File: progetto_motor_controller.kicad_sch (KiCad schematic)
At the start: 38 parts, among them J1 USB_B_Micro, J2 Conn_01x06, J3 Conn_01x04, J4 Screw_Terminal_01x03, J5 Conn_01x05, J6 Conn_02x10_Counter_Clockwise, J7 Conn_01x02, Q1 BSC022N04LSATMA1, SW1 SW_SPDT, U1 STM32F303RETx, U2 SN65HVD253D, U3 USBLC6-2P6, Y1 16MHz

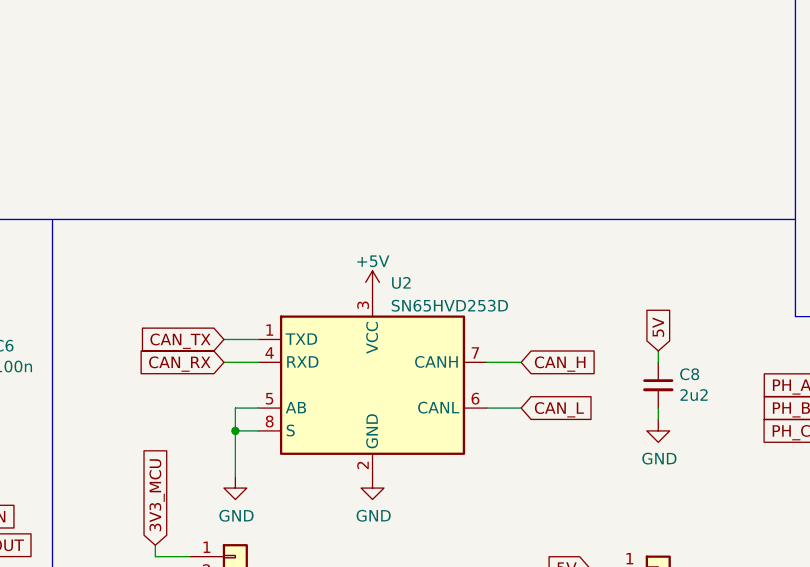
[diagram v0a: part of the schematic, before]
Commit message: added local symbol library
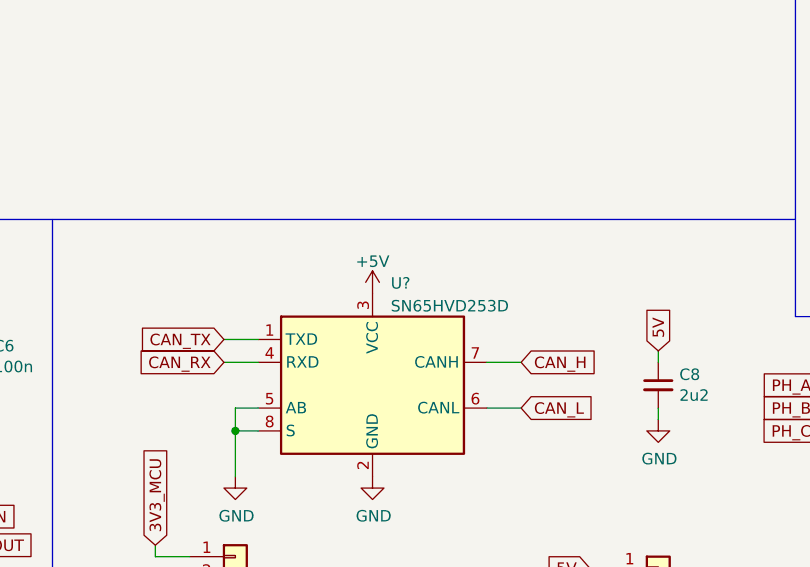
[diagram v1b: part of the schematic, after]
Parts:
- removed U2: SN65HVD253D, Package_SO:SOIC-8_3.9x4.9mm_P1.27mm, symbol Mylibrary:SN65HVD253D
- added U?: SN65HVD253D, Package_SO:SOIC-8_3.9x4.9mm_P1.27mm, symbol MyLibrary_PMSM:SN65HVD253D
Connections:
- net +5V: now also U?.3 (VCC)
- net CAN_H: now also U?.7 (CANH)
- net CAN_L: now also U?.6 (CANL)
- net CAN_RX: now also U?.4 (RXD)
- net CAN_TX: now also U?.1 (TXD)
- net GND: now also U?.2 (GND), U?.5 (NC), U?.8 (S)
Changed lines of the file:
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@@
     (pin "2")
   )
-  (symbol (lib_id "Mylibrary:SN65HVD253D") (at 149.86 90.17 0) (unit 1)
+  (symbol (lib_id "MyLibrary_PMSM:SN65HVD253D") (at 149.86 90.17 0) (unit 1)
     (in_bom yes) (on_board yes) (fields_autoplaced)
-    (property "Reference" "U2" (id 0) (at 151.8794 78.8502 0)
+    (property "Reference" "U?" (id 0) (at 151.8794 78.8502 0)
       (effects (font (size 1.27 1.27)) (justify left))
     )
@@
       (reference "U1") (unit 1) (value "STM32F303RETx") (footprint "Package_QFP:LQFP-64_10x10mm_P0.5mm")
     )
-    (path "/8331f48a-2afc-42bc-8008-84b452f97299"
-      (reference "U2") (unit 1) (value "SN65HVD253D") (footprint "Package_SO:SOIC-8_3.9x4.9mm_P1.27mm")
-    )
     (path "/00000000-0000-0000-0000-000061e1e007"
       (reference "U3") (unit 1) (value "USBLC6-2P6") (footprint "Package_TO_SOT_SMD:SOT-666")
     )
-    (path "/00000000-0000-0000-0000-000061cd02c2/00000000-0000-0000-0000-000061f8f6c5"
-      (reference "U4") (unit 1) (value "TMC6140") (footprint "")
-    )
-    (path "/00000000-0000-0000-0000-000061cd02c2/a6ec7d6b-e580-4409-8382-f30dedf5c393"
-      (reference "U5") (unit 1) (value "TSC2011") (footprint "")
-    )
-    (path "/00000000-0000-0000-0000-000061cd02c2/a291bac3-b45e-4638-a199-dbcaf18b2f09"
-      (reference "U6") (unit 1) (value "TSC2011") (footprint "")
-    )
-    (path "/1dc60600-5235-4456-91bf-a196642211fa/88a5c5b9-979a-4750-8fbf-0849978dd288"
-      (reference "U7") (unit 1) (value "MYRGC07506") (footprint "")
-    )
-    (path "/1dc60600-5235-4456-91bf-a196642211fa/6308fd98-fb59-4a41-97f1-92d9ad46298d"
-      (reference "U8") (unit 1) (value "TLV707") (footprint "")
+    (path "/00000000-0000-0000-0000-000061cd02c2/3359e259-3a3c-4aa4-8732-3dbaa9867503"
+      (reference "U?") (unit 1) (value "TSC2011") (footprint "")
+    )
+    (path "/00000000-0000-0000-0000-000061cd02c2/612a78e7-cc68-4577-b241-2d6ade45da87"
+      (reference "U?") (unit 1) (value "TMC6140") (footprint "")
+    )
+    (path "/1dc60600-5235-4456-91bf-a196642211fa/7902e9cd-4be0-4e1c-b27c-519fb539f14c"
+      (reference "U?") (unit 1) (value "TLV707") (footprint "")
+    )
+    (path "/00000000-0000-0000-0000-000061cd02c2/7c94c38e-623f-41eb-bdd6-5171cfc8b42f"
+      (reference "U?") (unit 1) (value "TSC2011") (footprint "")
+    )
+    (path "/80b39198-0427-4a2c-87f3-1492d50638db"
+      (reference "U?") (unit 1) (value "SN65HVD253D") (footprint "Package_SO:SOIC-8_3.9x4.9mm_P1.27mm")
+    )
+    (path "/1dc60600-5235-4456-91bf-a196642211fa/f139b3a3-5b4a-4b3f-8883-678a3f953d6f"
+      (reference "U?") (unit 1) (value "MYRGC07506_1") (footprint "")
     )
     (path "/00000000-0000-0000-0000-000061caf110"

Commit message: Third commit
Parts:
- gave numbers to parts that had none: 1
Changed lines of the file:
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@@
   (symbol (lib_id "MyLibrary_PMSM:SN65HVD253D") (at 149.86 90.17 0) (unit 1)
     (in_bom yes) (on_board yes) (fields_autoplaced)
-    (property "Reference" "U?" (id 0) (at 151.8794 78.8502 0)
+    (property "Reference" "U2" (id 0) (at 151.8794 78.8502 0)
       (effects (font (size 1.27 1.27)) (justify left))
     )
@@
       (reference "U1") (unit 1) (value "STM32F303RETx") (footprint "Package_QFP:LQFP-64_10x10mm_P0.5mm")
     )
+    (path "/80b39198-0427-4a2c-87f3-1492d50638db"
+      (reference "U2") (unit 1) (value "SN65HVD253D") (footprint "Package_SO:SOIC-8_3.9x4.9mm_P1.27mm")
+    )
     (path "/00000000-0000-0000-0000-000061e1e007"
       (reference "U3") (unit 1) (value "USBLC6-2P6") (footprint "Package_TO_SOT_SMD:SOT-666")
     )
+    (path "/00000000-0000-0000-0000-000061cd02c2/612a78e7-cc68-4577-b241-2d6ade45da87"
+      (reference "U4") (unit 1) (value "TMC6140") (footprint "MyLibrary:TMC6140-LA")
+    )
     (path "/00000000-0000-0000-0000-000061cd02c2/3359e259-3a3c-4aa4-8732-3dbaa9867503"
-      (reference "U?") (unit 1) (value "TSC2011") (footprint "")
-    )
-    (path "/00000000-0000-0000-0000-000061cd02c2/612a78e7-cc68-4577-b241-2d6ade45da87"
-      (reference "U?") (unit 1) (value "TMC6140") (footprint "")
+      (reference "U5") (unit 1) (value "TSC2011") (footprint "")
+    )
+    (path "/00000000-0000-0000-0000-000061cd02c2/7c94c38e-623f-41eb-bdd6-5171cfc8b42f"
+      (reference "U6") (unit 1) (value "TSC2011") (footprint "")
+    )
+    (path "/1dc60600-5235-4456-91bf-a196642211fa/f139b3a3-5b4a-4b3f-8883-678a3f953d6f"
+      (reference "U7") (unit 1) (value "MYRGC07506_1") (footprint "MyLibrary:Murata_picoBK")
     )
     (path "/1dc60600-5235-4456-91bf-a196642211fa/7902e9cd-4be0-4e1c-b27c-519fb539f14c"
-      (reference "U?") (unit 1) (value "TLV707") (footprint "")
-    )
-    (path "/00000000-0000-0000-0000-000061cd02c2/7c94c38e-623f-41eb-bdd6-5171cfc8b42f"
-      (reference "U?") (unit 1) (value "TSC2011") (footprint "")
-    )
-    (path "/80b39198-0427-4a2c-87f3-1492d50638db"
-      (reference "U?") (unit 1) (value "SN65HVD253D") (footprint "Package_SO:SOIC-8_3.9x4.9mm_P1.27mm")
-    )
-    (path "/1dc60600-5235-4456-91bf-a196642211fa/f139b3a3-5b4a-4b3f-8883-678a3f953d6f"
-      (reference "U?") (unit 1) (value "MYRGC07506_1") (footprint "")
+      (reference "U8") (unit 1) (value "TLV707") (footprint "MyLibrary:TLV707")
     )
     (path "/00000000-0000-0000-0000-000061caf110"

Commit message: added footprints
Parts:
- C8: footprint Capacitor_SMD:C_0402_1005Metric -> Capacitor_SMD:C_0603_1608Metric
- D4: footprint (none) -> Diode_SMD:D_SOD-323
- J2: footprint (none) -> Connector_Molex:Molex_Micro-Latch_53253-0670_1x06_P2.00mm_Vertical
- J3: footprint (none) -> Connector_Molex:Molex_Micro-Latch_53253-0470_1x04_P2.00mm_Vertical
- J5: footprint (none) -> Connector_Molex:Molex_Micro-Latch_53253-0570_1x05_P2.00mm_Vertical
- J6: footprint (none) -> Connector_JST:JST_PHD_S20B-PHDSS_2x10_P2.00mm_Horizontal
- J7: footprint (none) -> Connector_Molex:Molex_Micro-Latch_53253-0270_1x02_P2.00mm_Vertical
- Q1: footprint (none) -> MyLibrary:TDSON-8-6

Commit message: fourth commit
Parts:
- Q1: footprint MyLibrary:TDSON-8-6 -> MyLibrary:TDSON-8-6_copy
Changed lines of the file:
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@@
       (effects (font (size 1.27 1.27)) (justify left) hide)
     )
-    (property "Footprint" "MyLibrary:TDSON-8-6" (id 2) (at 259.08 105.41 0)
+    (property "Footprint" "MyLibrary:TDSON-8-6_copy" (id 2) (at 259.08 105.41 0)
       (effects (font (size 1.27 1.27)) hide)
     )
@@
     )
     (path "/68e088c0-f509-4963-a8c2-5f250da94fd0"
-      (reference "Q1") (unit 1) (value "BSC022N04LSATMA1") (footprint "MyLibrary:TDSON-8-6")
+      (reference "Q1") (unit 1) (value "BSC022N04LSATMA1") (footprint "MyLibrary:TDSON-8-6_copy")
     )
     (path "/00000000-0000-0000-0000-000061cd02c2/00000000-0000-0000-0000-000061d22286"
-      (reference "Q2") (unit 1) (value "BSC022N04LSATMA1") (footprint "MyLibrary:TDSON-8-6")
+      (reference "Q2") (unit 1) (value "BSC022N04LSATMA1") (footprint "MyLibrary:TDSON-8-6_copy")
     )
     (path "/00000000-0000-0000-0000-000061cd02c2/00000000-0000-0000-0000-000061d29f39"
-      (reference "Q3") (unit 1) (value "BSC022N04LSATMA1") (footprint "MyLibrary:TDSON-8-6")
+      (reference "Q3") (unit 1) (value "BSC022N04LSATMA1") (footprint "MyLibrary:TDSON-8-6_copy")
     )
     (path "/00000000-0000-0000-0000-000061cd02c2/00000000-0000-0000-0000-000061d31002"
-      (reference "Q4") (unit 1) (value "BSC022N04LSATMA1") (footprint "MyLibrary:TDSON-8-6")
+      (reference "Q4") (unit 1) (value "BSC022N04LSATMA1") (footprint "MyLibrary:TDSON-8-6_copy")
     )
     (path "/00000000-0000-0000-0000-000061cd02c2/00000000-0000-0000-0000-000061d31008"
-      (reference "Q5") (unit 1) (value "BSC022N04LSATMA1") (footprint "MyLibrary:TDSON-8-6")
+      (reference "Q5") (unit 1) (value "BSC022N04LSATMA1") (footprint "MyLibrary:TDSON-8-6_copy")
     )
     (path "/00000000-0000-0000-0000-000061cd02c2/00000000-0000-0000-0000-000061d36beb"
-      (reference "Q6") (unit 1) (value "BSC022N04LSATMA1") (footprint "MyLibrary:TDSON-8-6")
+      (reference "Q6") (unit 1) (value "BSC022N04LSATMA1") (footprint "MyLibrary:TDSON-8-6_copy")
     )
     (path "/00000000-0000-0000-0000-000061cd02c2/00000000-0000-0000-0000-000061d36bf1"
-      (reference "Q7") (unit 1) (value "BSC022N04LSATMA1") (footprint "MyLibrary:TDSON-8-6")
+      (reference "Q7") (unit 1) (value "BSC022N04LSATMA1") (footprint "MyLibrary:TDSON-8-6_copy")
     )
     (path "/1dc60600-5235-4456-91bf-a196642211fa/77da2cca-802e-41d0-b76d-7e6565304ae6"
@@
     )
     (path "/00000000-0000-0000-0000-000061cd02c2/9ed30845-4c8a-41f9-bb5e-fbf0150b5925"
-      (reference "Q?") (unit 1) (value "BSC040N10NS5") (footprint "Package_TO_SOT_SMD:TDSON-8-1")
+      (reference "Q9") (unit 1) (value "BSC040N10NS5") (footprint "Package_TO_SOT_SMD:TDSON-8-1")
     )
     (path "/00000000-0000-0000-0000-000061cf6f81"

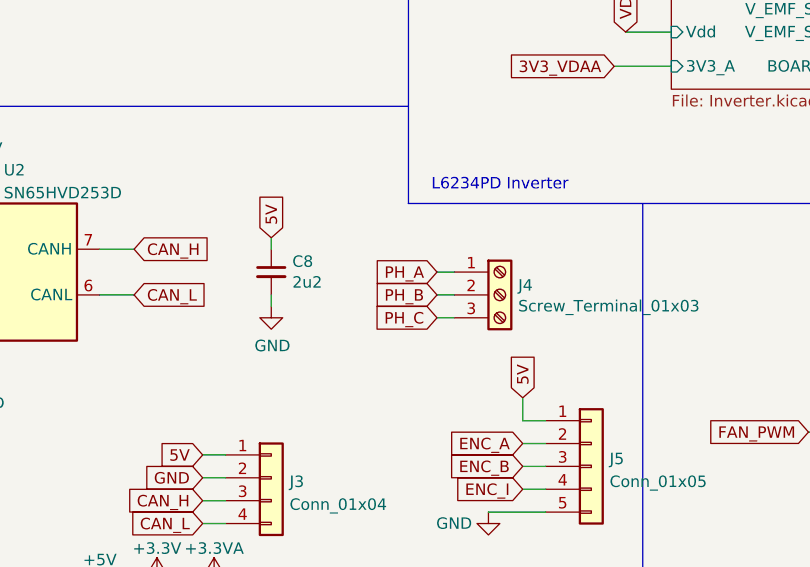
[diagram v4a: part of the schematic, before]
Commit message: started pcb layout
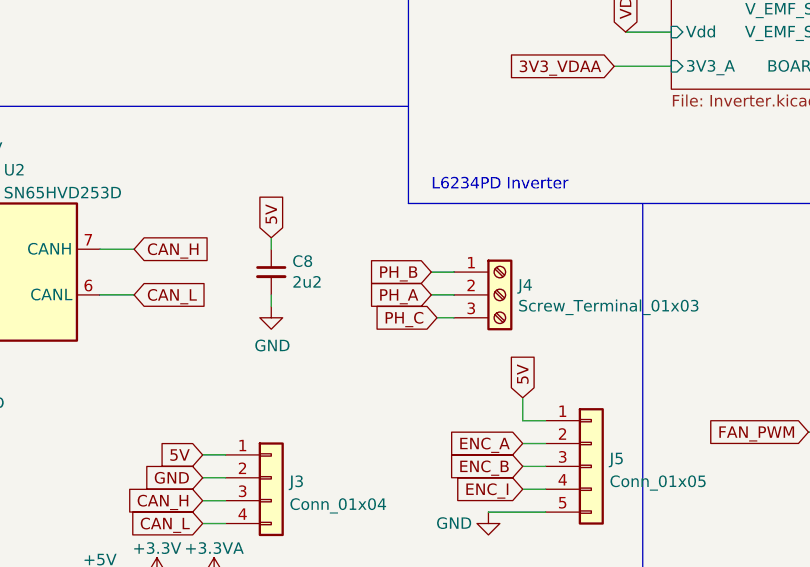
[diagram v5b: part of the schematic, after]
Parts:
- H1, H2, H3, H4: footprint MountingHole:MountingHole_4.3mm_M4_Pad -> MountingHole:MountingHole_3.2mm_M3_Pad_Via
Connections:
- net PH_A: now also J4.2 (Pin_2); no longer J4.1 (Pin_1)
- net PH_B: now also J4.1 (Pin_1); no longer J4.2 (Pin_2)
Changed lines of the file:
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@@
     (stroke (width 0) (type default) (color 0 0 0 0))
   )
-  (wire (pts (xy 200.025 92.71) (xy 201.93 92.71))
+  (wire (pts (xy 199.39 92.71) (xy 201.93 92.71))
     (stroke (width 0) (type default) (color 0 0 0 0))
   )
@@
     (stroke (width 0) (type default) (color 0 0 0 0))
   )
-  (wire (pts (xy 200.025 90.17) (xy 201.93 90.17))
+  (wire (pts (xy 199.39 90.17) (xy 201.93 90.17))
     (stroke (width 0) (type default) (color 0 0 0 0))
   )
@@
     )
   )
-  (global_label "PH_B" (shape input) (at 200.025 92.71 180) (fields_autoplaced)
-    (effects (font (size 1.27 1.27)) (justify right))
-    (property "Intersheet References" "${INTERSHEET_REFS}" (id 0) (at 24.13 -12.7 0)
+  (global_label "PH_B" (shape input) (at 199.39 90.17 180) (fields_autoplaced)
+    (effects (font (size 1.27 1.27)) (justify right))
+    (property "Intersheet References" "${INTERSHEET_REFS}" (id 0) (at 23.495 -15.24 0)
       (effects (font (size 1.27 1.27)) hide)
     )
@@
     )
   )
-  (global_label "PH_A" (shape input) (at 200.025 90.17 180) (fields_autoplaced)
-    (effects (font (size 1.27 1.27)) (justify right))
-    (property "Intersheet References" "${INTERSHEET_REFS}" (id 0) (at 24.13 -12.7 0)
+  (global_label "PH_A" (shape input) (at 199.39 92.71 180) (fields_autoplaced)
+    (effects (font (size 1.27 1.27)) (justify right))
+    (property "Intersheet References" "${INTERSHEET_REFS}" (id 0) (at 23.495 -10.16 0)
       (effects (font (size 1.27 1.27)) hide)
     )
@@
       (effects (font (size 1.27 1.27)) (justify left))
     )
-    (property "Footprint" "MountingHole:MountingHole_4.3mm_M4_Pad" (id 2) (at 136.525 168.275 0)
+    (property "Footprint" "MountingHole:MountingHole_3.2mm_M3_Pad_Via" (id 2) (at 136.525 168.275 0)
       (effects (font (size 1.27 1.27)) hide)
     )
@@
       (effects (font (size 1.27 1.27)) (justify left))
     )
-    (property "Footprint" "MountingHole:MountingHole_4.3mm_M4_Pad" (id 2) (at 136.525 174.625 0)
+    (property "Footprint" "MountingHole:MountingHole_3.2mm_M3_Pad_Via" (id 2) (at 136.525 174.625 0)
       (effects (font (size 1.27 1.27)) hide)
     )
@@
       (effects (font (size 1.27 1.27)) (justify left))
     )
-    (property "Footprint" "MountingHole:MountingHole_4.3mm_M4_Pad" (id 2) (at 136.525 180.975 0)
+    (property "Footprint" "MountingHole:MountingHole_3.2mm_M3_Pad_Via" (id 2) (at 136.525 180.975 0)
       (effects (font (size 1.27 1.27)) hide)
     )
@@
       (effects (font (size 1.27 1.27)) (justify left))
     )
-    (property "Footprint" "MountingHole:MountingHole_4.3mm_M4_Pad" (id 2) (at 136.525 187.325 0)
+    (property "Footprint" "MountingHole:MountingHole_3.2mm_M3_Pad_Via" (id 2) (at 136.525 187.325 0)
       (effects (font (size 1.27 1.27)) hide)
     )
@@
       (reference "#PWR035") (unit 1) (value "+3.3VA") (footprint "")
     )
+    (path "/1dc60600-5235-4456-91bf-a196642211fa/10316b78-14f6-4008-bf44-df0decf0c9a5"
+      (reference "#PWR036") (unit 1) (value "GND") (footprint "")
+    )
     (path "/739d06ed-e117-4e08-b12a-c2c864ed21d5"
       (reference "#PWR0101") (unit 1) (value "GND") (footprint "")
@@
     )
     (path "/00000000-0000-0000-0000-000061e81daf"
-      (reference "H1") (unit 1) (value "MountingHole_Pad") (footprint "MountingHole:MountingHole_4.3mm_M4_Pad")
+      (reference "H1") (unit 1) (value "MountingHole_Pad") (footprint "MountingHole:MountingHole_3.2mm_M3_Pad_Via")
     )
     (path "/00000000-0000-0000-0000-000061e82624"
-      (reference "H2") (unit 1) (value "MountingHole_Pad") (footprint "MountingHole:MountingHole_4.3mm_M4_Pad")
+      (reference "H2") (unit 1) (value "MountingHole_Pad") (footprint "MountingHole:MountingHole_3.2mm_M3_Pad_Via")
     )
     (path "/00000000-0000-0000-0000-000061e82824"
-      (reference "H3") (unit 1) (value "MountingHole_Pad") (footprint "MountingHole:MountingHole_4.3mm_M4_Pad")
+      (reference "H3") (unit 1) (value "MountingHole_Pad") (footprint "MountingHole:MountingHole_3.2mm_M3_Pad_Via")
     )
     (path "/00000000-0000-0000-0000-000061e82adc"
-      (reference "H4") (unit 1) (value "MountingHole_Pad") (footprint "MountingHole:MountingHole_4.3mm_M4_Pad")
+      (reference "H4") (unit 1) (value "MountingHole_Pad") (footprint "MountingHole:MountingHole_3.2mm_M3_Pad_Via")
     )
     (path "/00000000-0000-0000-0000-000061e1429f"

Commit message: rev_0.1
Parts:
- removed D3: LED_Small, LED_SMD:LED_0603_1608Metric, symbol Device:LED_Small
- removed J6: Conn_02x10_Counter_Clockwise, Connector_JST:JST_PHD_S20B-PHDSS_2x10_P2.00mm_Horizontal, symbol Connector_Generic:Conn_02x10_Counter_Clockwise
- removed R6: 1k5, Resistor_SMD:R_0603_1608Metric, symbol Device:R_Small
- removed SW1: SW_SPDT, Button_Switch_SMD:SW_SPDT_PCM12, symbol Switch:SW_SPDT
- added C39, C40, C41: 2u2, Capacitor_SMD:C_0603_1608Metric, symbol Device:C_Small
- added C42: 1u, Capacitor_SMD:C_0402_1005Metric, symbol Device:C_Small
- added C43: 10n, Capacitor_SMD:C_0402_1005Metric, symbol Device:C_Small
- added J6: Conn_02x10_Odd_Even, MyLibrary:JST_SHD_SM20B, symbol Connector_Generic:Conn_02x10_Odd_Even
- added J9: Conn_01x03, Connector_PinHeader_2.54mm:PinHeader_1x03_P2.54mm_Vertical, symbol Connector_Generic:Conn_01x03
- added R29, R30, R31, R32, R33, R34: 1k5, Resistor_SMD:R_0603_1608Metric, symbol Device:R_Small
- J2: footprint Connector_Molex:Molex_Micro-Latch_53253-0670_1x06_P2.00mm_Vertical -> Connector_JST_mod:JST_GH_SM06B-GHS-TB_06x1.25mm_Angled
- J3: footprint Connector_Molex:Molex_Micro-Latch_53253-0470_1x04_P2.00mm_Vertical -> Connector_JST_mod:JST_GH_SM04B-GHS-TB_04x1.25mm_Angled
- J5: footprint Connector_Molex:Molex_Micro-Latch_53253-0570_1x05_P2.00mm_Vertical -> Connector_JST_mod:JST_GH_SM05B-GHS-TB_05x1.25mm_Angled
- J7: footprint Connector_Molex:Molex_Micro-Latch_53253-0270_1x02_P2.00mm_Vertical -> Connector_JST_mod:JST_GH_SM02B-GHS-TB_02x1.25mm_Angled
- Q1: footprint MyLibrary:TDSON-8-6_copy -> Package_TO_SOT_SMD:SOT-23
- R1, R4, R7, R8: footprint Resistor_SMD:R_0402_1005Metric -> Resistor_SMD:R_0603_1608Metric
- U3: footprint Package_TO_SOT_SMD:SOT-666 -> Package_TO_SOT_SMD:SOT-363_SC-70-6
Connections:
- net +3.3VA: now also C42.1, C43.1
- net +3V3: now also J6.18 (Pin_18), J6.4 (Pin_4), J9.1 (Pin_1)
- net +5V: now also J5.5 (Pin_5), J6.2 (Pin_2), J6.20 (Pin_20), R29.2, R30.2, R31.2; no longer J5.1 (Pin_1)
- net CAN_H: now also J3.4 (Pin_4); no longer J3.3 (Pin_3)
- net CAN_L: now also J3.3 (Pin_3); no longer J3.4 (Pin_4)
- net ENC_A: now also C39.1, R31.1, R32.1; no longer J5.2 (Pin_2)
- net ENC_B: now also C40.1, R30.1, R33.1; no longer J5.3 (Pin_3)
- net ENC_I: now also C41.1, R29.1, R34.1; no longer J5.4 (Pin_4)
- net ERROR: now also J6.10 (Pin_10)
- net GND: now also J5.1 (Pin_1), C39.2, C40.2, C41.2, C42.2, C43.2, J6.1 (Pin_1), J6.15 (Pin_15), J6.16 (Pin_16), J6.17 (Pin_17), J6.19 (Pin_19), J6.3 (Pin_3), J9.3 (Pin_3); no longer J5.5 (Pin_5)
- net MISO: now also J6.5 (Pin_5)
- net MOSI: now also J6.7 (Pin_7)
- net NSS: now also J6.6 (Pin_6)
- net PH_A: now also J4.3 (Pin_3); no longer J4.2 (Pin_2)
- net PH_B: now also J4.2 (Pin_2); no longer J4.1 (Pin_1)
- net PH_C: now also J4.1 (Pin_1); no longer J4.3 (Pin_3)
- net PWM_HA: now also U1.10 (PC2); no longer U1.8 (PC0)
- net PWM_HC: now also U1.8 (PC0); no longer U1.10 (PC2)
- net PWM_IN_1: now also J6.12 (Pin_12)
- net PWM_IN_2: now also J6.14 (Pin_14)
- net PWM_LA: now also U1.27 (PB1); no longer U1.23 (PA7)
- net PWM_LC: now also U1.23 (PA7); no longer U1.27 (PB1)
- net SCK: now also J6.8 (Pin_8)
- net UART_RX: now also J6.11 (Pin_11)
- net UART_TX: now also J6.9 (Pin_9)
- net at R1.2: now also J9.2 (Pin_2)
- net LED_B: no longer names the net of U1.42 (PA9)
- new net EN: J6.13 (Pin_13)
- new net ENC_AA: J5.2 (Pin_2), R32.2
- new net ENC_BB: J5.3 (Pin_3), R33.2
- new net ENC_II: J5.4 (Pin_4), R34.2
- no-connect marks 13 -> 14
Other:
- sheet Power ports: added 3V3_MCU; removed none
- moved on the sheet: J3, R1
